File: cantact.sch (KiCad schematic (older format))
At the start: 38 parts, among them J1 USB_C_Receptacle_USB2.0, J2 Conn_01x04, J3 Conn_01x06, SW1 SW_SPST, SW2 SW_DPDT_x2, U1 NJM2871, U2 STM32F042C6Ux, U3 MCP2562-E-MF, Y1 Resonator

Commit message: 電源LEDの配置いじった
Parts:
- removed SW1: SW_SPST, Button_Switch_SMD:SW_SPST_B3U-1000P, symbol Switch:SW_SPST
- added SW1: SKRPACE010, Button_Switch_SMD_my:ALPS_SKRPAxE010, symbol mylib:SKRPACE010
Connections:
- net at R7.1, U2.44 (PF11): now also SW1.3
- net CAN_-: now reaches J2.3 (Pin_3), R9.1, U3.6 (CANL)
- net CAN_+: now reaches J2.2 (Pin_2), SW2.2 (B), U3.7 (CANH)
- net at R4.2: now also SW1.1
- no-connect marks 32 -> 34
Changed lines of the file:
@@
 	4750 2800 4850 2800
-$Comp
-L Switch:SW_SPST SW1
-U 1 1 5FAB2BCC
-P 4500 3300
-F 0 "SW1" H 4500 3535 50  0000 C CNN
-F 1 "SW_SPST" H 4500 3444 50  0000 C CNN
-F 2 "Button_Switch_SMD:SW_SPST_B3U-1000P" H 4500 3300 50  0001 C CNN
-F 3 "~" H 4500 3300 50  0001 C CNN
-	1    4500 3300
-	1    0    0    -1
-$EndComp
-Wire Wire Line
-	4700 3300 5350 3300
-Wire Wire Line
-	4300 3300 4100 3300
 $Comp
 L Switch:SW_DPDT_x2 SW2
@@
 NoConn ~ 9300 1900
 NoConn ~ 9000 1300
+Text Label 9650 3900 0    50   ~ 0
+CAN_+
+Text Label 9650 4000 0    50   ~ 0
+CAN_-
+$Comp
+L mylib:SKRPACE010 SW1
+U 1 1 5FB5B91C
+P 4500 3500
+F 0 "SW1" V 4454 3301 50  0000 R CNN
+F 1 "SKRPACE010" V 4545 3301 50  0000 R CNN
+F 2 "Button_Switch_SMD_my:ALPS_SKRPAxE010" V 4450 3500 60  0001 C CNN
+F 3 "http://www.alps.com/prod/info/J/HTML/Tact/SurfaceMount/SKRP/SKRP_list.html" V 4450 3500 60  0001 C CNN
+	1    4500 3500
+	0    -1   1    0
+$EndComp
+Wire Wire Line
+	4100 3300 4400 3300
+Wire Wire Line
+	4600 3300 5350 3300
+NoConn ~ 4400 3700
+NoConn ~ 4600 3700
 $EndSCHEMATC

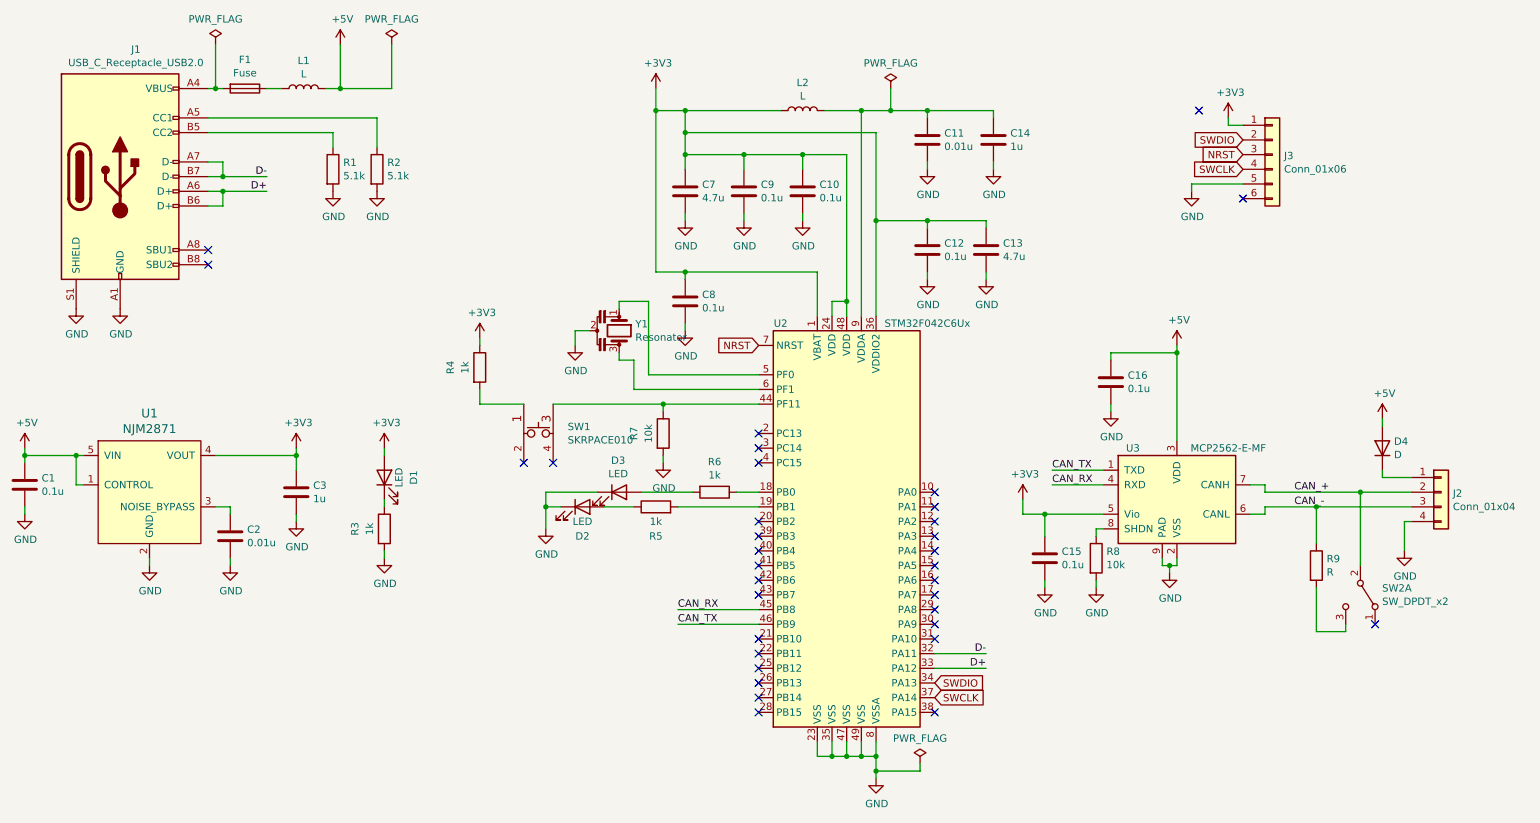
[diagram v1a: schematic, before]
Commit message: 不要なシルクは全部非表示にした
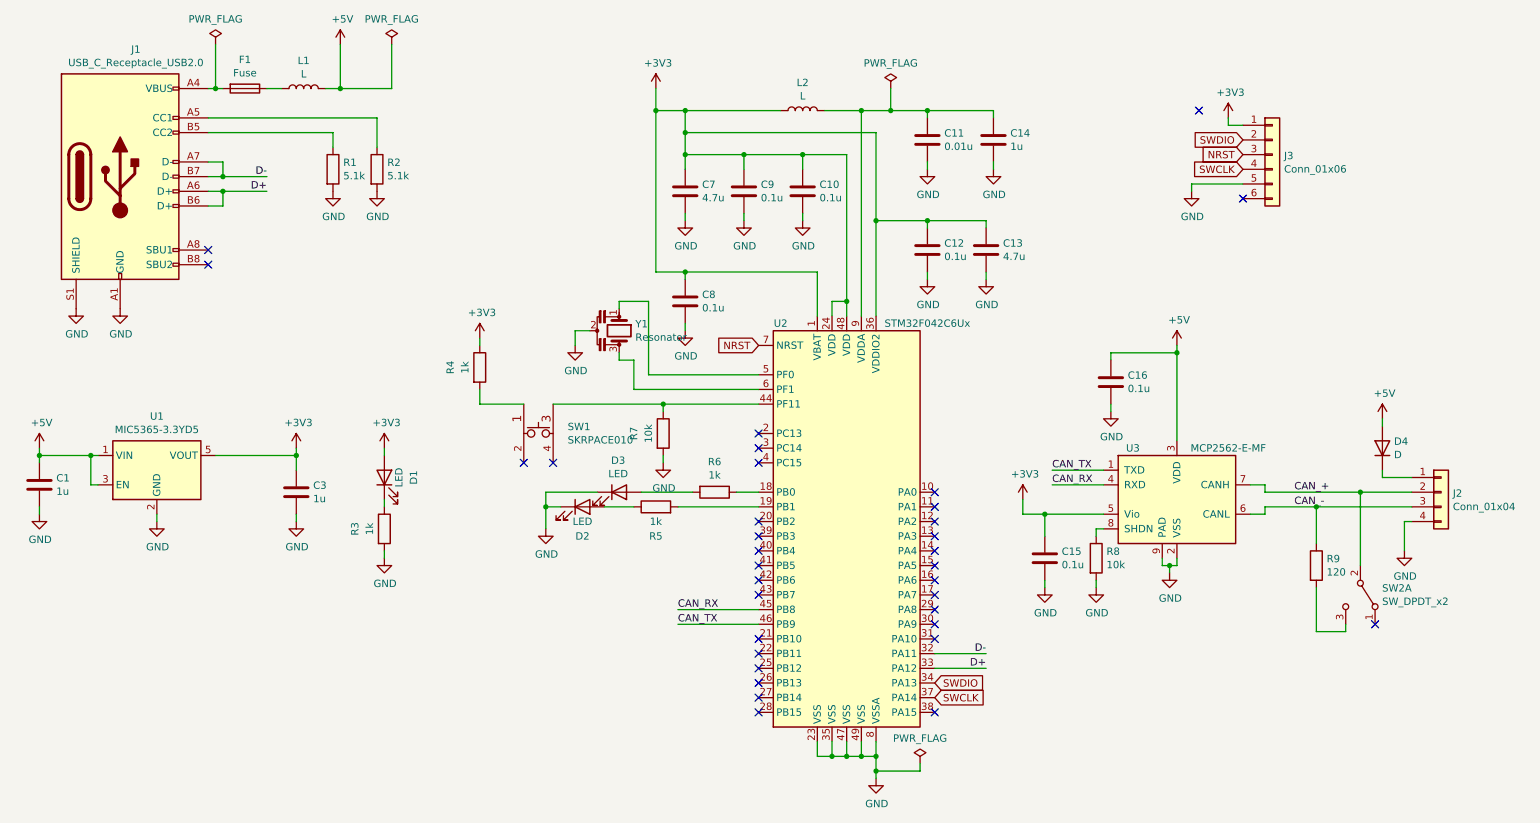
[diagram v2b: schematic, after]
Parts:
- removed C2: 0.01u, Capacitor_SMD:C_0402_1005Metric, symbol Device:C
- removed U1: NJM2871, Package_TO_SOT_SMD:SOT-23-5, symbol mylib:NJM2871
- added U1: MIC5365-3.3YD5, Package_TO_SOT_SMD:SOT-23-5, symbol Regulator_Linear:MIC5365-3.3YD5
- C1: value 0.1u -> 1u
- R9: value R -> 120
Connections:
- net +3V3: now also U1.5 (VOUT)
- net +5V: now also U1.1 (VIN), U1.3 (EN)
- net GND: now also U1.2 (GND)
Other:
- moved on the sheet: C1
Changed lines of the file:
@@
 Connection ~ 8850 2950
-$Comp
-L mylib:NJM2871 U1
-U 1 1 5D49797A
-P 1850 3850
-F 0 "U1" H 1850 4337 60  0000 C CNN
-F 1 "NJM2871" H 1850 4231 60  0000 C CNN
-F 2 "Package_TO_SOT_SMD:SOT-23-5" H 1950 3700 60  0001 C CNN
-F 3 "" H 1950 3700 60  0001 C CNN
-	1    1850 3850
-	1    0    0    -1
-$EndComp
-$Comp
-L Device:C C2
-U 1 1 5D499104
-P 2400 4200
-F 0 "C2" H 2515 4246 50  0000 L CNN
-F 1 "0.01u" H 2515 4155 50  0000 L CNN
-F 2 "Capacitor_SMD:C_0402_1005Metric" H 2438 4050 50  0001 C CNN
-F 3 "~" H 2400 4200 50  0001 C CNN
-	1    2400 4200
-	1    0    0    -1
-$EndComp
-Wire Wire Line
-	2300 4000 2400 4000
-Wire Wire Line
-	2400 4000 2400 4050
 $Comp
 L power:GND #PWR0125
 U 1 1 5D4AADD5
-P 1850 4400
-F 0 "#PWR0125" H 1850 4150 50  0001 C CNN
-F 1 "GND" H 1855 4227 50  0000 C CNN
-F 2 "" H 1850 4400 50  0001 C CNN
-F 3 "" H 1850 4400 50  0001 C CNN
-	1    1850 4400
-	1    0    0    -1
-$EndComp
-Wire Wire Line
-	1850 4400 1850 4350
-$Comp
-L power:GND #PWR0126
-U 1 1 5D4AECFC
-P 2400 4400
-F 0 "#PWR0126" H 2400 4150 50  0001 C CNN
-F 1 "GND" H 2405 4227 50  0000 C CNN
-F 2 "" H 2400 4400 50  0001 C CNN
-F 3 "" H 2400 4400 50  0001 C CNN
-	1    2400 4400
-	1    0    0    -1
-$EndComp
-Wire Wire Line
-	2400 4400 2400 4350
+P 1900 4100
+F 0 "#PWR0125" H 1900 3850 50  0001 C CNN
+F 1 "GND" H 1905 3927 50  0000 C CNN
+F 2 "" H 1900 4100 50  0001 C CNN
+F 3 "" H 1900 4100 50  0001 C CNN
+	1    1900 4100
+	1    0    0    -1
+$EndComp
+Wire Wire Line
+	1900 4100 1900 4050
 $Comp
 L Device:C C3
@@
 L Device:C C1
 U 1 1 5D4BFEAA
-P 1000 3850
-F 0 "C1" H 885 3896 50  0000 R CNN
-F 1 "0.1u" H 885 3805 50  0000 R CNN
-F 2 "Capacitor_SMD:C_0402_1005Metric" H 1038 3700 50  0001 C CNN
-F 3 "~" H 1000 3850 50  0001 C CNN
-	1    1000 3850
+P 1100 3850
+F 0 "C1" H 985 3896 50  0000 R CNN
+F 1 "1u" H 985 3805 50  0000 R CNN
+F 2 "Capacitor_SMD:C_0402_1005Metric" H 1138 3700 50  0001 C CNN
+F 3 "~" H 1100 3850 50  0001 C CNN
+	1    1100 3850
 	-1   0    0    -1
 $EndComp
 Wire Wire Line
-	1400 3650 1350 3650
-Wire Wire Line
-	1000 3650 1000 3700
-Wire Wire Line
-	1400 3850 1350 3850
-Wire Wire Line
-	1350 3850 1350 3650
-Connection ~ 1350 3650
-Wire Wire Line
-	1350 3650 1000 3650
+	1500 3650 1450 3650
+Wire Wire Line
+	1100 3650 1100 3700
+Wire Wire Line
+	1500 3850 1450 3850
+Wire Wire Line
+	1450 3850 1450 3650
+Connection ~ 1450 3650
+Wire Wire Line
+	1450 3650 1100 3650
 $Comp
 L power:GND #PWR0129
 U 1 1 5D4C9893
-P 1000 4050
-F 0 "#PWR0129" H 1000 3800 50  0001 C CNN
-F 1 "GND" H 1005 3877 50  0000 C CNN
-F 2 "" H 1000 4050 50  0001 C CNN
-F 3 "" H 1000 4050 50  0001 C CNN
-	1    1000 4050
-	1    0    0    -1
-$EndComp
-Wire Wire Line
-	1000 4050 1000 4000
+P 1100 4050
+F 0 "#PWR0129" H 1100 3800 50  0001 C CNN
+F 1 "GND" H 1105 3877 50  0000 C CNN
+F 2 "" H 1100 4050 50  0001 C CNN
+F 3 "" H 1100 4050 50  0001 C CNN
+	1    1100 4050
+	1    0    0    -1
+$EndComp
+Wire Wire Line
+	1100 4050 1100 4000
 $Comp
 L power:+5V #PWR0130
 U 1 1 5D4CE607
-P 1000 3600
-F 0 "#PWR0130" H 1000 3450 50  0001 C CNN
-F 1 "+5V" H 1015 3773 50  0000 C CNN
-F 2 "" H 1000 3600 50  0001 C CNN
-F 3 "" H 1000 3600 50  0001 C CNN
-	1    1000 3600
-	1    0    0    -1
-$EndComp
-Wire Wire Line
-	1000 3600 1000 3650
-Connection ~ 1000 3650
+P 1100 3600
+F 0 "#PWR0130" H 1100 3450 50  0001 C CNN
+F 1 "+5V" H 1115 3773 50  0000 C CNN
+F 2 "" H 1100 3600 50  0001 C CNN
+F 3 "" H 1100 3600 50  0001 C CNN
+	1    1100 3600
+	1    0    0    -1
+$EndComp
+Wire Wire Line
+	1100 3600 1100 3650
+Connection ~ 1100 3650
 $Comp
 L power:+3V3 #PWR0131
@@
 P 9800 4400
 F 0 "R9" H 9870 4446 50  0000 L CNN
-F 1 "R" H 9870 4355 50  0000 L CNN
+F 1 "120" H 9870 4355 50  0000 L CNN
 F 2 "Resistor_SMD:R_0603_1608Metric" V 9730 4400 50  0001 C CNN
 F 3 "~" H 9800 4400 50  0001 C CNN
@@
 NoConn ~ 4400 3700
 NoConn ~ 4600 3700
+$Comp
+L Regulator_Linear:MIC5365-3.3YD5 U1
+U 1 1 5FBC9208
+P 1900 3750
+F 0 "U1" H 1900 4117 50  0000 C CNN
+F 1 "MIC5365-3.3YD5" H 1900 4026 50  0000 C CNN
+F 2 "Package_TO_SOT_SMD:SOT-23-5" H 1900 4100 50  0001 C CNN
+F 3 "http://ww1.microchip.com/downloads/en/DeviceDoc/mic5365.pdf" H 1650 4000 50  0001 C CNN
+	1    1900 3750
+	1    0    0    -1
+$EndComp
 $EndSCHEMATC
